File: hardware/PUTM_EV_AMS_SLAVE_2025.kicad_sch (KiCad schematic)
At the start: 9 parts, among them J1 M80-5100405, J2 M80-5100405, J4 IDC24

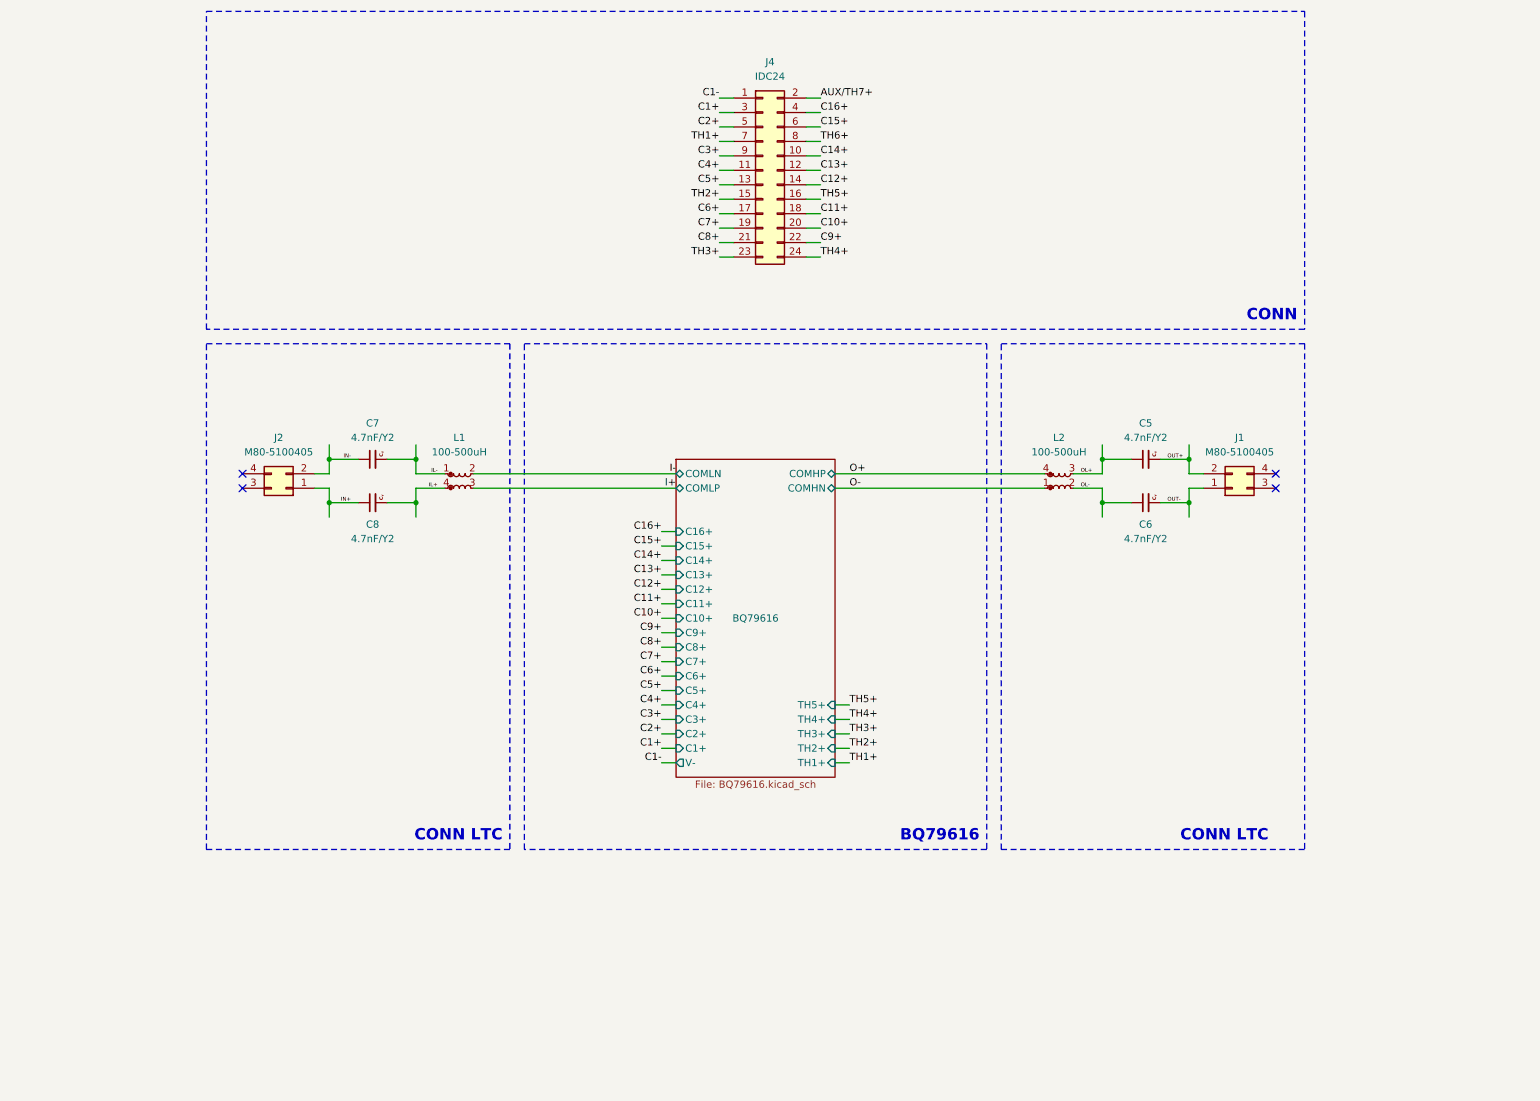
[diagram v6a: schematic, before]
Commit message: some visual touch ups, added aux diodes for checking comm with IC, temp meas section, fliped the connector to the other side etc.
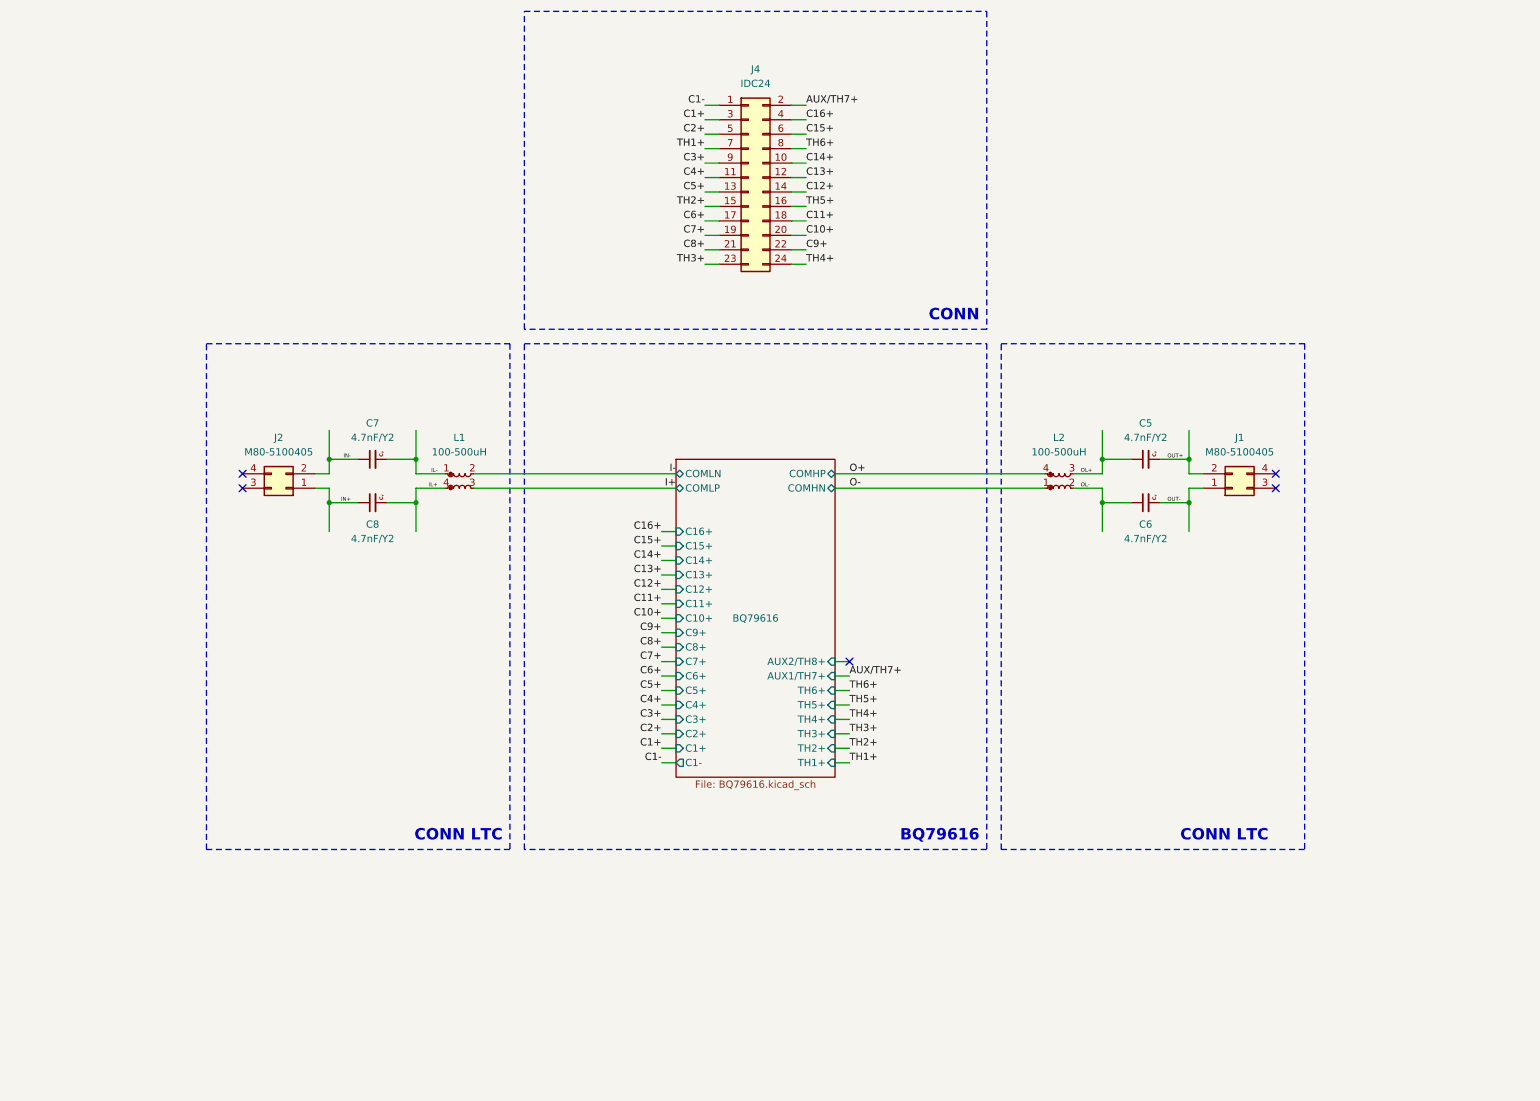
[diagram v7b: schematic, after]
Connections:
- no-connect marks 4 -> 5
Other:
- sheet BQ79616 ports: added AUX1/TH7+, AUX2/TH8+, C1-, TH6+; removed V-
- moved on the sheet: J4

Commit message: pcb layout 99.9% done - all sections named and placed also some initial routing
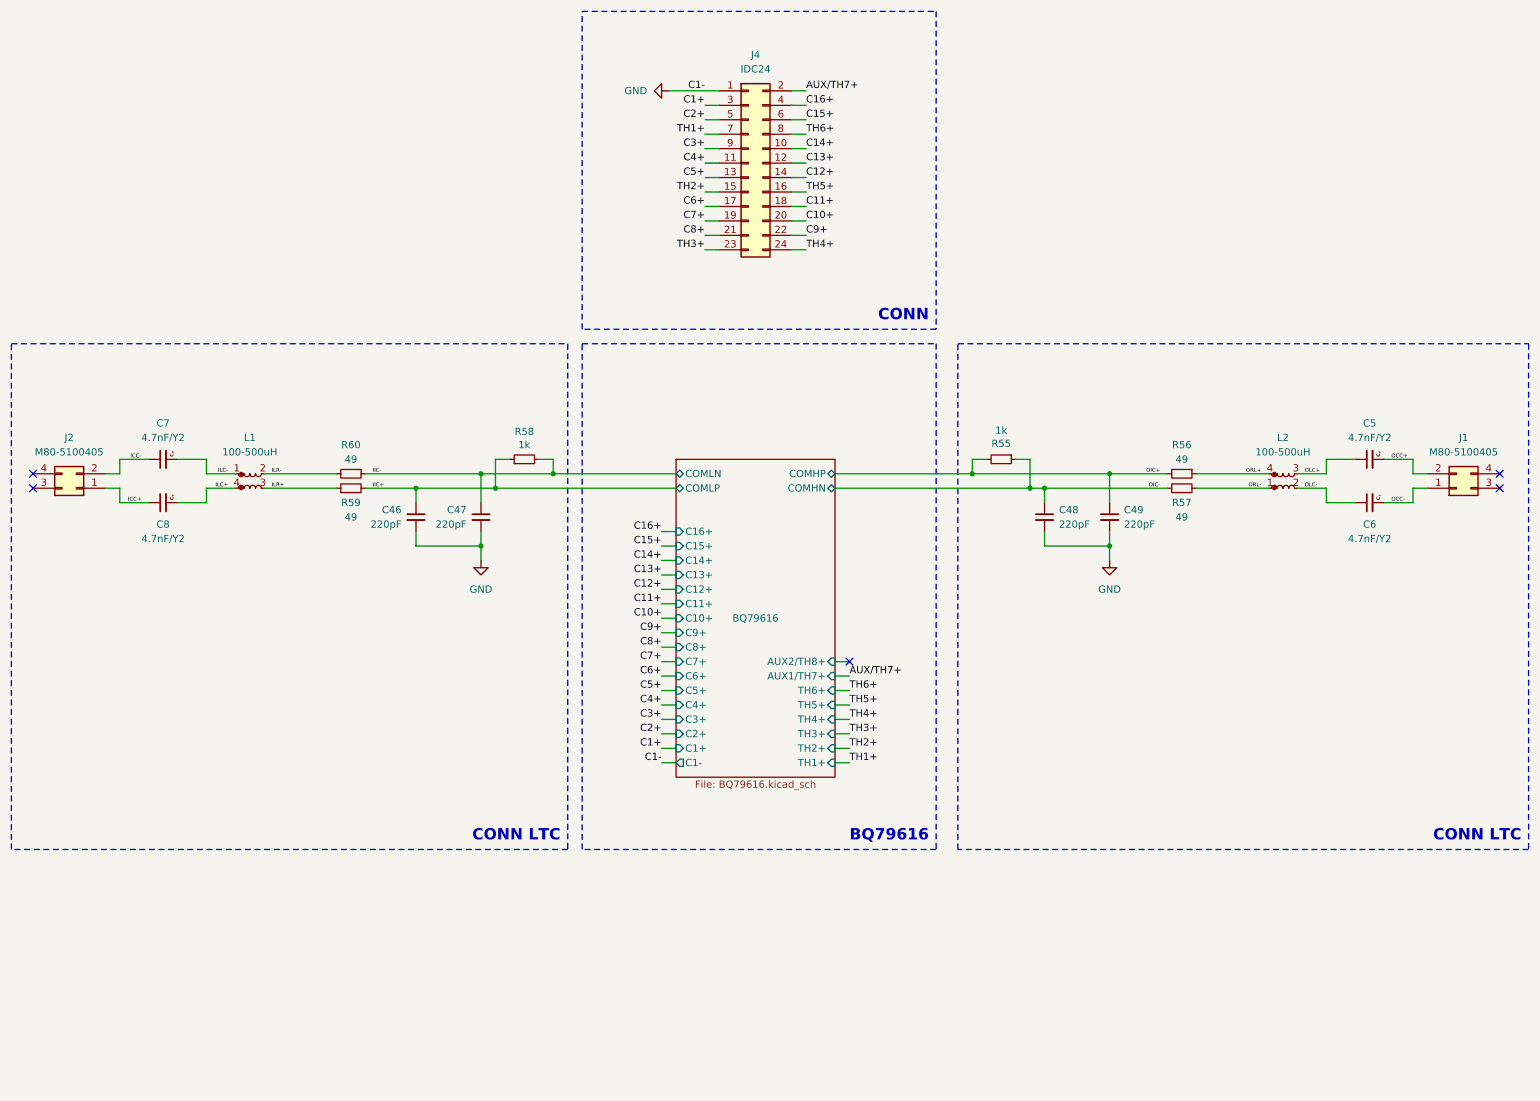
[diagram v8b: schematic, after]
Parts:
- added C46, C47, C48, C49: 220pF, Capacitor_SMD:C_0603_1608Metric, symbol Device:C_Small
- added R55, R58: 1k, Resistor_SMD:R_0603_1608Metric, symbol PUTM_EV_BMS_HV_Slave_2021-rescue:R_Small-Device
- added R56, R57, R59, R60: 49, Resistor_SMD:R_0603_1608Metric, symbol PUTM_EV_BMS_HV_Slave_2021-rescue:R_Small-Device
- L1, L2: Mouser Price/Stock (none) -> https://www.mouser.pl/ProductDetail/Pulse-Electronics/PE-18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
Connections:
- net C1- renamed GND
- net GND: now also C46.2, C47.2, C48.2, C49.2
- net I+ renamed ILR+
- net ILR+: now also R59.1
- net I- renamed ILR-
- net ILR-: now also R60.2
- net IL+ renamed ILC+
- net IL- renamed ILC-
- net IN+ renamed ICC+
- net IN- renamed ICC-
- net O+ renamed ORL+
- net ORL+: now also R56.1
- net O- renamed ORL-
- net ORL-: now also R57.2
- net OL+ renamed OLC+
- net OL- renamed OLC-
- net OUT+ renamed OCC+
- net OUT- renamed OCC-
- new net IIC+: C46.1, R58.1, R59.2
- new net IIC-: C47.1, R58.2, R60.1
- new net OIC+: C49.1, R55.2, R56.2
- new net OIC-: C48.1, R55.1, R57.1
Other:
- moved on the sheet: C5, C6, C7, C8, J1, J2, J4, L1, L2
